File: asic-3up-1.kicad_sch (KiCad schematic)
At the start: 66 parts, among them J14 Conn_01x01, J15 Conn_01x01, J5 Conn_01x01, J7 Conn_01x01, U48 MCP1824T-1202E/OT, U49 MCP1824T-1202E/OT, U50 MCP1824T-1202E/OT, U51 MCP1824T-0802E, U52 MCP1824T-0802E, U53 MCP1824T-0802E, U54 BM1362AC_MODE1, U55 BM1362AC_MODE0, U56 BM1362AC_MODE1

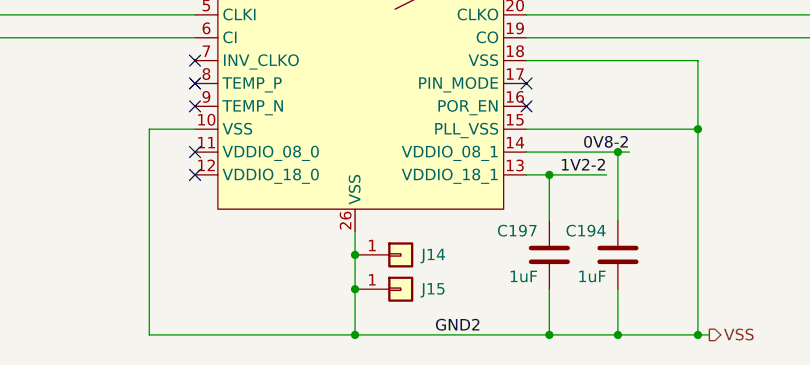
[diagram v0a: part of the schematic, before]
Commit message: remove all power pads, replace with planes, including on back layer. regenerate BOM
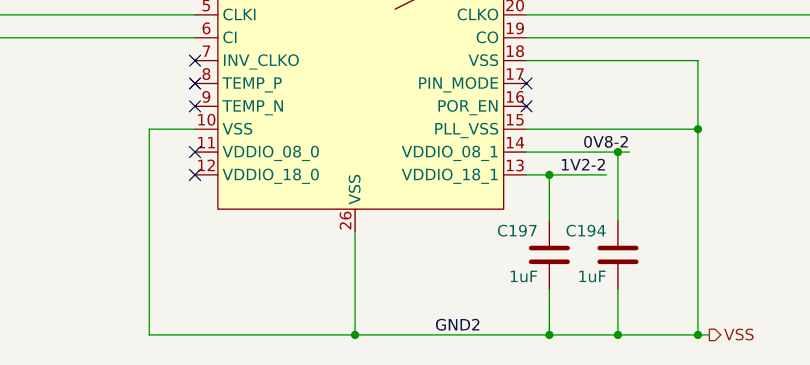
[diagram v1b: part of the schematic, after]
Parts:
- removed J14: Conn_01x01, emberone:14x9_powertab_L, symbol Connector_Generic:Conn_01x01
- removed J15: Conn_01x01, emberone:14x9_powertab_R, symbol Connector_Generic:Conn_01x01
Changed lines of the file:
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@@
 	)
 	(junction
-		(at 248.92 207.01)
-		(diameter 0)
-		(color 0 0 0 0)
-	)
-	(junction
 		(at 57.15 124.46)
 		(diameter 0.9144)
@@
 	)
 	(junction
-		(at 248.92 210.82)
-		(diameter 0)
-		(color 0 0 0 0)
-	)
-	(junction
 		(at 226.06 139.7)
 		(diameter 0)
@@
 	(wire
 		(pts
-			(xy 248.92 207.01) (xy 248.92 210.82)
-		)
-		(stroke
-			(width 0)
-			(type default)
-		)
-	)
-	(wire
-		(pts
 			(xy 57.15 138.43) (xy 87.63 138.43)
 		)
@@
 	(wire
 		(pts
-			(xy 248.92 204.47) (xy 248.92 207.01)
+			(xy 248.92 204.47) (xy 248.92 215.9)
 		)
 		(stroke
@@
 	(wire
 		(pts
-			(xy 248.92 210.82) (xy 248.92 215.9)
-		)
-		(stroke
-			(width 0)
-			(type default)
-		)
-	)
-	(wire
-		(pts
 			(xy 124.46 68.58) (xy 127 68.58)
 		)
@@
 	)
 	(symbol
-		(lib_id "Connector_Generic:Conn_01x01")
-		(at 254 207.01 0)
-		(unit 1)
-		(exclude_from_sim no)
-		(in_bom yes)
-		(on_board yes)
-		(dnp no)
-		(property "Reference" "J14"
-			(at 256.286 207.01 0)
-			(effects
-				(font
-					(size 1.27 1.27)
-				)
-				(justify left)
-			)
-		)
-		(property "Value" "Conn_01x01"
-			(at 256.54 208.2799 0)
-			(effects
-				(font
-					(size 1.27 1.27)
-				)
-				(justify left)
-				(hide yes)
-			)
-		)
-		(property "Footprint" "emberone:14x9_powertab_L"
-			(at 254 207.01 0)
-			(effects
-				(font
-					(size 1.27 1.27)
-				)
-				(hide yes)
-			)
-		)
-		(property "Datasheet" "~"
-			(at 254 207.01 0)
-			(effects
-				(font
-					(size 1.27 1.27)
-				)
-				(hide yes)
-			)
-		)
-		(property "Description" "powertab"
-			(at 254 207.01 0)
-			(effects
-				(font
-					(size 1.27 1.27)
-				)
-				(hide yes)
-			)
-		)
-		(pin "1"
-		)
-		(instances
-			(project "emberone"
-				(path "/b036224c-4cdf-48cc-81df-19bc5283ebd2/1041e984-4167-4ef3-8410-dcacf0440a69"
-					(reference "J14")
-					(unit 1)
-				)
-			)
-		)
-	)
-	(symbol
 		(lib_id "Connector:TestPoint")
 		(at 160.02 124.46 270)
@@
 					(unit 1)
 				)
-			)
-		)
-	)
-	(symbol
-		(lib_id "Connector_Generic:Conn_01x01")
-		(at 254 210.82 0)
-		(unit 1)
-		(exclude_from_sim no)
-		(in_bom yes)
-		(on_board yes)
-		(dnp no)
-		(property "Reference" "J15"
-			(at 256.286 210.82 0)
-			(effects
-				(font
-					(size 1.27 1.27)
-				)
-				(justify left)
-			)
-		)
-		(property "Value" "Conn_01x01"
-			(at 256.54 212.0899 0)
-			(effects
-				(font
-					(size 1.27 1.27)
-				)
-				(justify left)
-				(hide yes)
-			)
-		)
-		(property "Footprint" "emberone:14x9_powertab_R"
-			(at 254 210.82 0)
-			(effects
-				(font
-					(size 1.27 1.27)
-				)
-				(hide yes)
-			)
-		)
-		(property "Datasheet" "~"
-			(at 254 210.82 0)
-			(effects
-				(font
-					(size 1.27 1.27)
-				)
-				(hide yes)
-			)
-		)
-		(property "Description" "powertab"
-			(at 254 210.82 0)
-			(effects
-				(font
-					(size 1.27 1.27)
-				)
-				(hide yes)
-			)
-		)
-		(pin "1"
-		)
-		(instances
-			(project "emberone"
-				(path "/b036224c-4cdf-48cc-81df-19bc5283ebd2/1041e984-4167-4ef3-8410-dcacf0440a69"
-					(reference "J15")
-					(unit 1)
-				)
